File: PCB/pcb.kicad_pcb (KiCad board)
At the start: 2 copper layers, 64.8 x 74.5 mm, 64 parts, among them J1 EXT POWER, J10 RGBW LED, J11 I2C Breakout, J2 Screw_Terminal_01x03, J3 RJ45, J4 RJ45, J5 EXT_BTN1, J6 EXT_BTN1, J7 Screw_Terminal_01x03, J8 Screw_Terminal_01x03, J9 Screw_Terminal_01x03, SW2 Factory Reset, SW3 User, SW4 User, U1 SN74LVC1G125DCK, U2 ADS1115IDGS, U4 AP63205WU, U5 AP2114-3.3, U6 LM358, U7 TJA1051T-3, U8 MOUDLE-SEEEDUINO-XIAO-ESP32S3

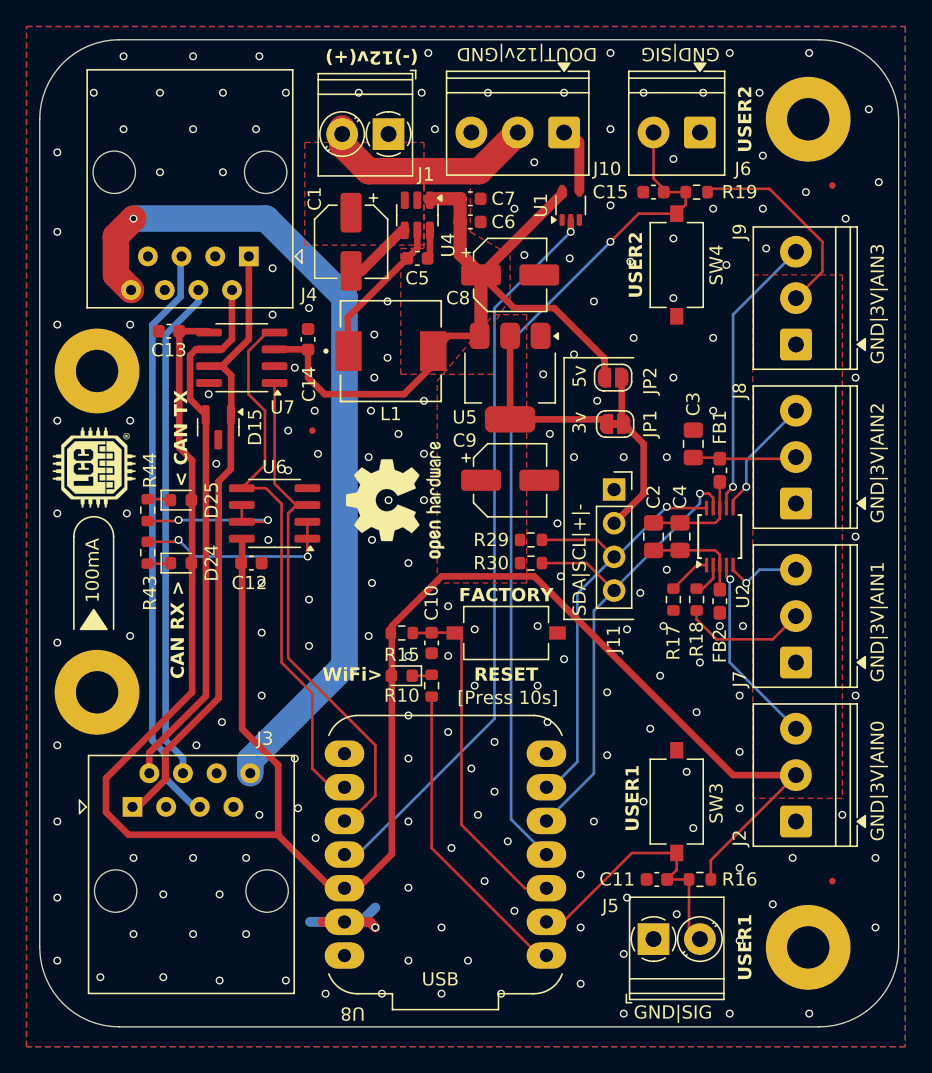
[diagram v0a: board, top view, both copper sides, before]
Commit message: Update PCB files with latest rev, export fabrication outputs, update README and add documentation photos
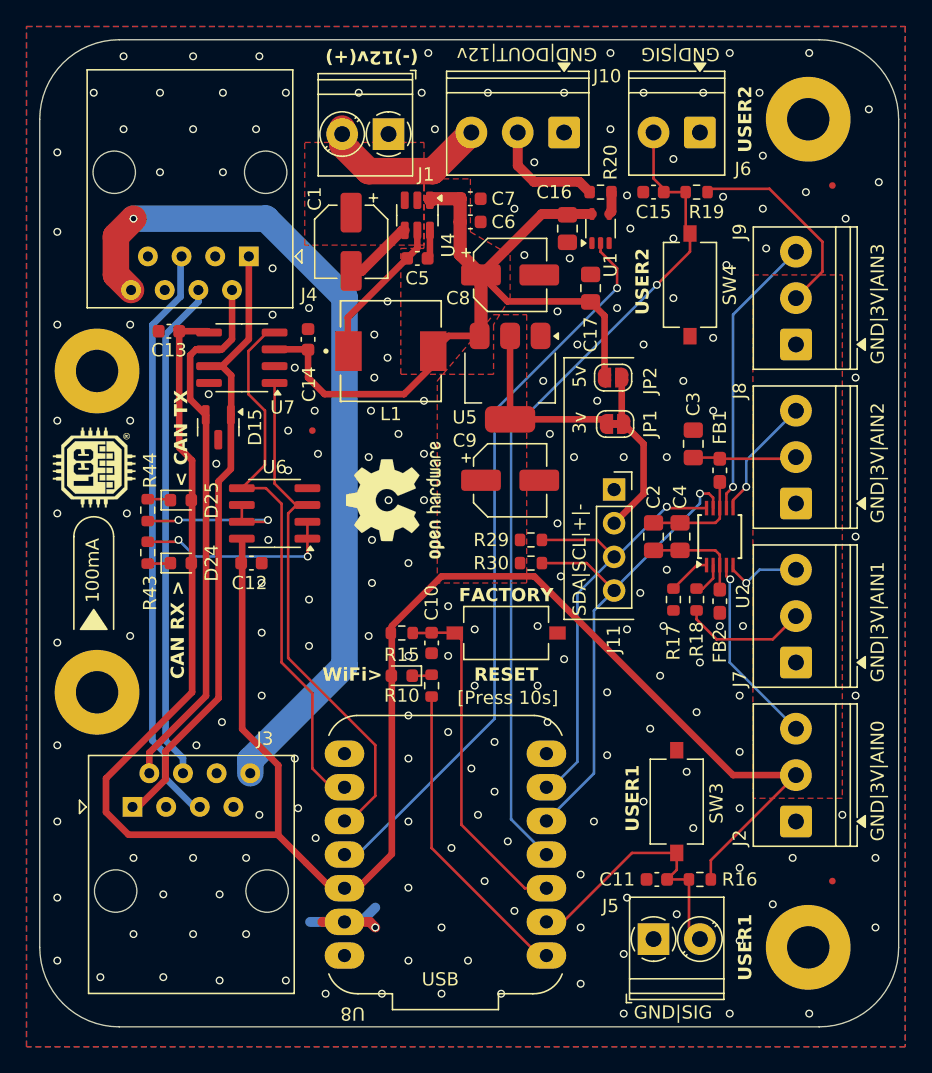
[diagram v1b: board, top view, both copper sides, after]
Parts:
- added C16: 10uF, Capacitor_SMD:C_0805_2012Metric_Pad1.18x1.45mm_HandSolder, F.Cu at (83.2, 63.2)
- added C17: 1uF, Capacitor_SMD:C_0805_2012Metric_Pad1.18x1.45mm_HandSolder, F.Cu at (85.0, 67.8)
- added R20: 100, Resistor_SMD:R_0603_1608Metric, F.Cu at (85.8, 60.5)
- moved U1 2.85 mm to (85.8, 63.2)
- moved SW4 1.80 mm to (92.5, 67.5)
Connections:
- J10 pad 1: NEOPIXEL_DOUT -> GND
- J10 pad 2: +12v -> NEOPIXEL_DOUT
- J10 pad 3: GND -> +12v
- U1 pad 4: NEOPIXEL_DOUT -> Net-(R20-Pad2)
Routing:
- net +12v: track 16.1 -> 12.6 mm
- net NEOPIXEL_DOUT: track 5.29 -> 8.75 mm
- net +5V: track 55.9 -> 59.2 mm
- net Net-(R20-Pad2): track 0.00 -> 1.72 mm
- net USER_BTN_1: track 64.8 -> 63.4 mm
- net GND: vias 188 -> 189
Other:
- board text added: "GND|DOUT|12v"
- board text removed: "DOUT|12v|GND"
